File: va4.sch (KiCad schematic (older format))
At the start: 12 parts, among them J1 LED, J2 MJ-4PP-9, SW1 RESET_SWITCH, SW2 SW_PUSH, SW3 SW_PUSH, SW4 SW_PUSH, SW5 SW_PUSH, U1 ProMicro

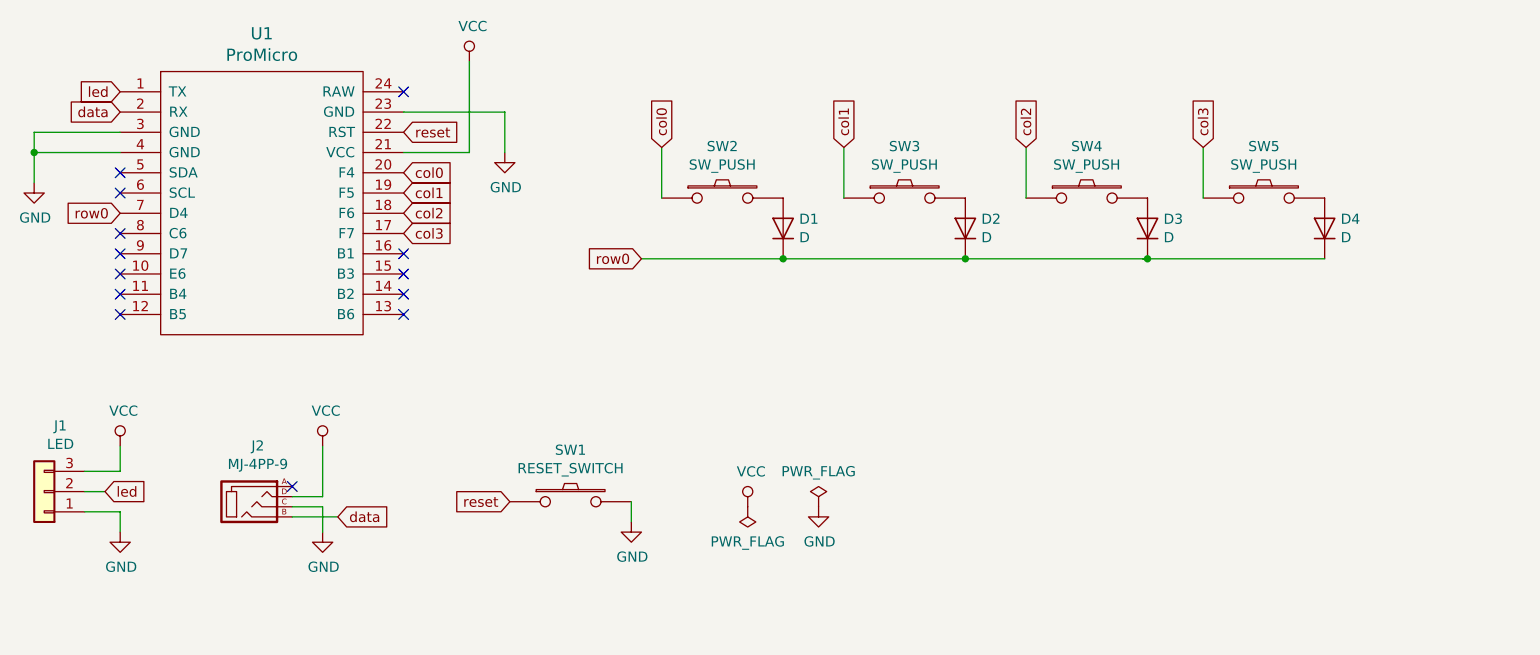
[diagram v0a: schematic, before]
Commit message: Rotary encoder with mx SW5
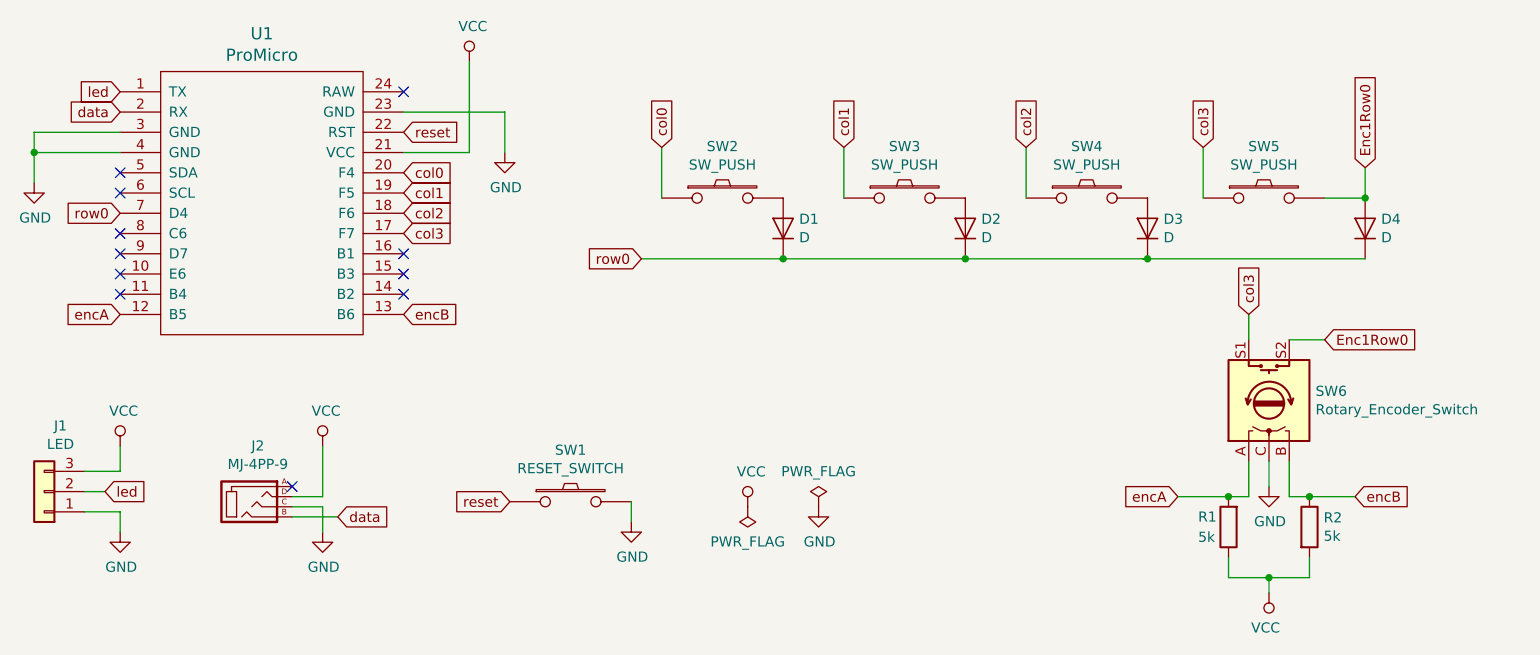
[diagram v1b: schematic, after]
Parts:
- added R1, R2: 5k, Resistors:0805, symbol Device:R
- added SW6: Rotary_Encoder_Switch, AcheronHardware:ALPS_EC11E, symbol Device:Rotary_Encoder_Switch
- SW5: footprint kbd:MX_ALPS_PG1350_noLed -> Keebio-Parts:Hybrid_PCB_100H
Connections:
- net labels added: Enc1Row0, encA, encB
- wire segments 28 -> 44
- no-connect marks 13 -> 11
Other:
- moved on the sheet: D4
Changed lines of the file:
@@
 EESchema Schematic File Version 4
 LIBS:va4-cache
-EELAYER 26 0
+EELAYER 29 0
 EELAYER END
 $Descr A4 11693 8268
@@
 NoConn ~ 2025 3050
 NoConn ~ 2025 3150
-NoConn ~ 2025 3250
-NoConn ~ 3425 3250
 NoConn ~ 3425 3150
 NoConn ~ 3425 3050
@@
 F 0 "SW5" H 7675 2930 50  0000 C CNN
 F 1 "SW_PUSH" H 7675 2839 50  0000 C CNN
-F 2 "kbd:MX_ALPS_PG1350_noLed" H 7675 2675 50  0001 C CNN
+F 2 "Keebio-Parts:Hybrid_PCB_100H" H 7675 2675 50  0001 C CNN
 F 3 "" H 7675 2675 50  0000 C CNN
 	1    7675 2675
@@
 L Device:D D4
 U 1 1 5C05486C
-P 7975 2825
-F 0 "D4" V 8021 2746 50  0000 R CNN
-F 1 "D" V 7930 2746 50  0000 R CNN
-F 2 "kbd:D3_TH_SMD" H 7975 2825 50  0001 C CNN
-F 3 "~" H 7975 2825 50  0001 C CNN
-	1    7975 2825
+P 8175 2825
+F 0 "D4" V 8221 2746 50  0000 R CNN
+F 1 "D" V 8130 2746 50  0000 R CNN
+F 2 "kbd:D3_TH_SMD" H 8175 2825 50  0001 C CNN
+F 3 "~" H 8175 2825 50  0001 C CNN
+	1    8175 2825
 	0    -1   -1   0
 $EndComp
@@
 Connection ~ 7100 2975
 Wire Wire Line
-	7100 2975 7975 2975
-Wire Wire Line
 	7075 2975 7100 2975
 Wire Wire Line
 	6200 2975 7100 2975
+$Comp
+L Device:Rotary_Encoder_Switch SW6
+U 1 1 5D6F2CCE
+P 7700 3675
+F 0 "SW6" V 7746 3445 50  0000 R CNN
+F 1 "Rotary_Encoder_Switch" V 7655 3445 50  0000 R CNN
+F 2 "AcheronHardware:ALPS_EC11E" H 7550 3835 50  0001 C CNN
+F 3 "~" H 7700 3935 50  0001 C CNN
+	1    7700 3675
+	0    -1   -1   0
+$EndComp
+$Comp
+L Device:R R1
+U 1 1 5D6F4E9B
+P 7500 4300
+F 0 "R1" H 7650 4250 50  0000 R CNN
+F 1 "5k" H 7650 4350 50  0000 R CNN
+F 2 "Resistors:0805" V 7430 4300 50  0001 C CNN
+F 3 "~" H 7500 4300 50  0001 C CNN
+	1    7500 4300
+	-1   0    0    1
+$EndComp
+$Comp
+L Device:R R2
+U 1 1 5D6F5ECD
+P 7900 4300
+F 0 "R2" H 7970 4346 50  0000 L CNN
+F 1 "5k" H 7970 4255 50  0000 L CNN
+F 2 "Resistors:0805" V 7830 4300 50  0001 C CNN
+F 3 "~" H 7900 4300 50  0001 C CNN
+	1    7900 4300
+	1    0    0    -1
+$EndComp
+$Comp
+L power:GND #PWR01
+U 1 1 5D6F61D9
+P 7700 4100
+F 0 "#PWR01" H 7700 3850 50  0001 C CNN
+F 1 "GND" H 7705 3927 50  0000 C CNN
+F 2 "" H 7700 4100 50  0001 C CNN
+F 3 "" H 7700 4100 50  0001 C CNN
+	1    7700 4100
+	1    0    0    -1
+$EndComp
+Wire Wire Line
+	7700 3975 7700 4100
+Wire Wire Line
+	7975 2675 8175 2675
+Wire Wire Line
+	7100 2975 8175 2975
+Connection ~ 8175 2675
+Text GLabel 8175 2525 1    50   Input ~ 0
+Enc1Row0
+Wire Wire Line
+	8175 2675 8175 2525
+Text GLabel 7975 3375 2    50   Input ~ 0
+Enc1Row0
+Wire Wire Line
+	7800 3375 7975 3375
+Text GLabel 7600 3250 1    50   Input ~ 0
+col3
+Wire Wire Line
+	7600 3375 7600 3250
+Wire Wire Line
+	7600 3975 7600 4150
+Wire Wire Line
+	7600 4150 7500 4150
+Wire Wire Line
+	7800 3975 7800 4150
+Wire Wire Line
+	7800 4150 7900 4150
+Wire Wire Line
+	7500 4450 7500 4550
+Wire Wire Line
+	7900 4450 7900 4550
+Wire Wire Line
+	7500 4550 7700 4550
+Wire Wire Line
+	7700 4550 7700 4625
+Connection ~ 7700 4550
+Wire Wire Line
+	7700 4550 7900 4550
+$Comp
+L power:VCC #PWR02
+U 1 1 5D7008C5
+P 7700 4625
+F 0 "#PWR02" H 7700 4475 50  0001 C CNN
+F 1 "VCC" H 7717 4798 50  0000 C CNN
+F 2 "" H 7700 4625 50  0001 C CNN
+F 3 "" H 7700 4625 50  0001 C CNN
+	1    7700 4625
+	-1   0    0    1
+$EndComp
+Wire Wire Line
+	7500 4150 7250 4150
+Connection ~ 7500 4150
+Wire Wire Line
+	7900 4150 8125 4150
+Connection ~ 7900 4150
+Text GLabel 2025 3250 0    50   Input ~ 0
+encA
+Text GLabel 7250 4150 0    50   Input ~ 0
+encA
+Text GLabel 8125 4150 2    50   Input ~ 0
+encB
+Text GLabel 3425 3250 2    50   Input ~ 0
+encB
 $EndSCHEMATC

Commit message: choc mx hybrid with rotary encoder on SW5
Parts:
- SW5: footprint Keebio-Parts:Hybrid_PCB_100H -> kbd:MX_ALPS_PG1350_noLed
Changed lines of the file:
@@
 F 0 "SW5" H 7675 2930 50  0000 C CNN
 F 1 "SW_PUSH" H 7675 2839 50  0000 C CNN
-F 2 "Keebio-Parts:Hybrid_PCB_100H" H 7675 2675 50  0001 C CNN
+F 2 "kbd:MX_ALPS_PG1350_noLed" H 7675 2675 50  0001 C CNN
 F 3 "" H 7675 2675 50  0000 C CNN
 	1    7675 2675
